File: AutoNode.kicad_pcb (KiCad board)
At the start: 4 copper layers, 144.8 x 106.7 mm, 130 parts, among them IC10 MAX17263LETD+T, IC12 TPS22975, IC14 W25Q64FWSSIG, IC19 TPS22975, IC2 MCP73871, IC3 HDC2080, IC4 TPS2013A, IC5 CAT25160VI-GT3, IC6 SN74LVC244A, IC7 LP38691-ADJ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

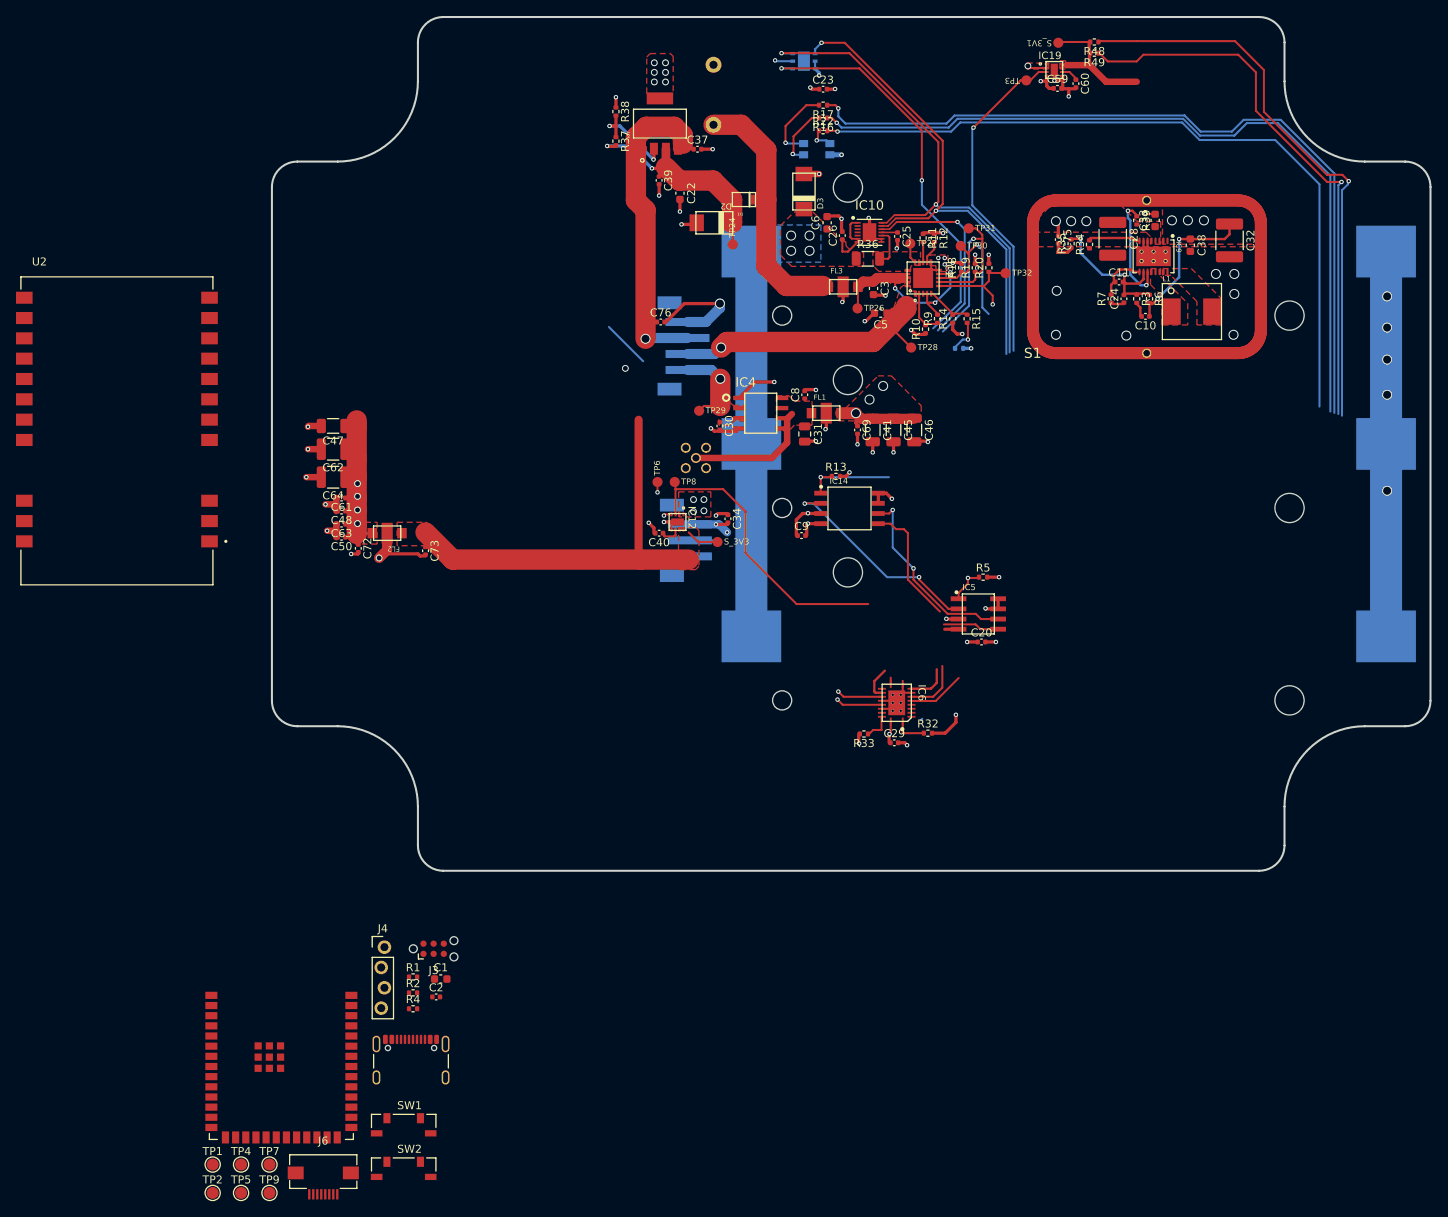
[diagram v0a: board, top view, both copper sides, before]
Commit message: fixed up silk screen text sizes, board outline and mounting holes
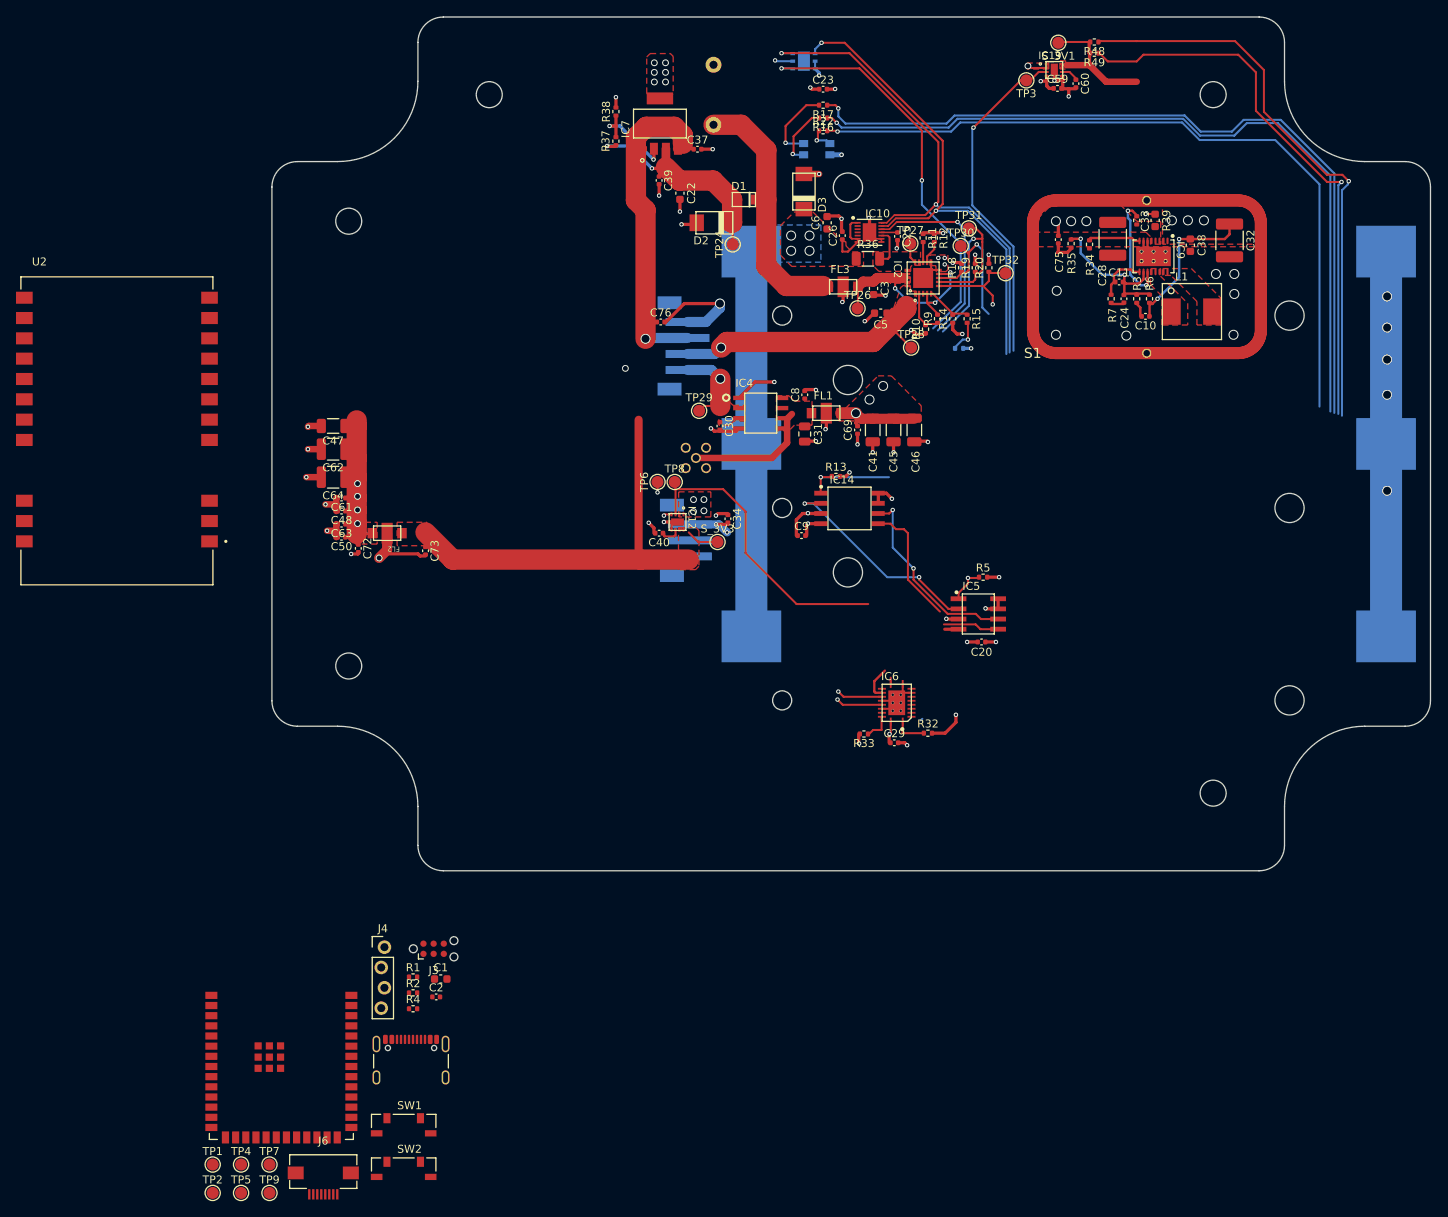
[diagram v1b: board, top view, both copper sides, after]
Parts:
- S_3V1, S_3V3, TP24, TP26, TP27, TP28, TP29, TP3, TP30, TP31, TP32, TP6, TP8: footprint autonode:PAD.03X.05 -> TestPoint:TestPoint_Pad_D1.5mm
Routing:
- net GND: track 184.6 -> 195.4 mm, vias 67 -> 68
- net /Power Input/VOUT: track 10.9 -> 0.00 mm, vias 1 -> 0
- net /Radio/SCK: track 12.9 -> 5.76 mm
- net /Radio/TXEN: track 11.2 -> 4.18 mm
- net (no net): track 6.07 -> 0.00 mm
- net /Radio/RXEN: track 5.96 -> 0.80 mm
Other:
- outline, holes or cut-outs redrawn
